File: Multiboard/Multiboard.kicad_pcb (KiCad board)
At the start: 2 copper layers, 120 x 120 mm, 115 parts, among them J1 Conn_01x20_Socket, J2 Conn_01x20_Socket, J3 Debug, J4 USB_C_Receptacle_USB2.0_16P, Q1 Q_NMOS, Q10 Q_NMOS, Q11 Q_NMOS, Q12 Q_NMOS, Q13 Q_NMOS, Q14 Q_NMOS, Q15 Q_NMOS, Q16 Q_NMOS, Q17 Q_NMOS, Q18 Q_NMOS, Q2 Q_NMOS, Q3 Q_NMOS, Q4 Q_NMOS, Q5 Q_NMOS, Q6 Q_NMOS, Q7 Q_NMOS, Q8 Q_NMOS, Q9 Q_NMOS, SW1 BOOT0, SW2 NRST, SW3 SW_SPST, SW4 SW_SPST, SW5 SW_SPST, SW6 SW_SPST, SW7 SW_SPST, SW8 KEY, U1 STM32F411RET6, U2 MAX662AESA_T, U3 MCP1792x-3302xCB, U4 USART1, U5 I2C1, U6 SPI1, U7 ADC, U8 GPIO-PWM, Y1 32.768KHz, Y2 25MHz

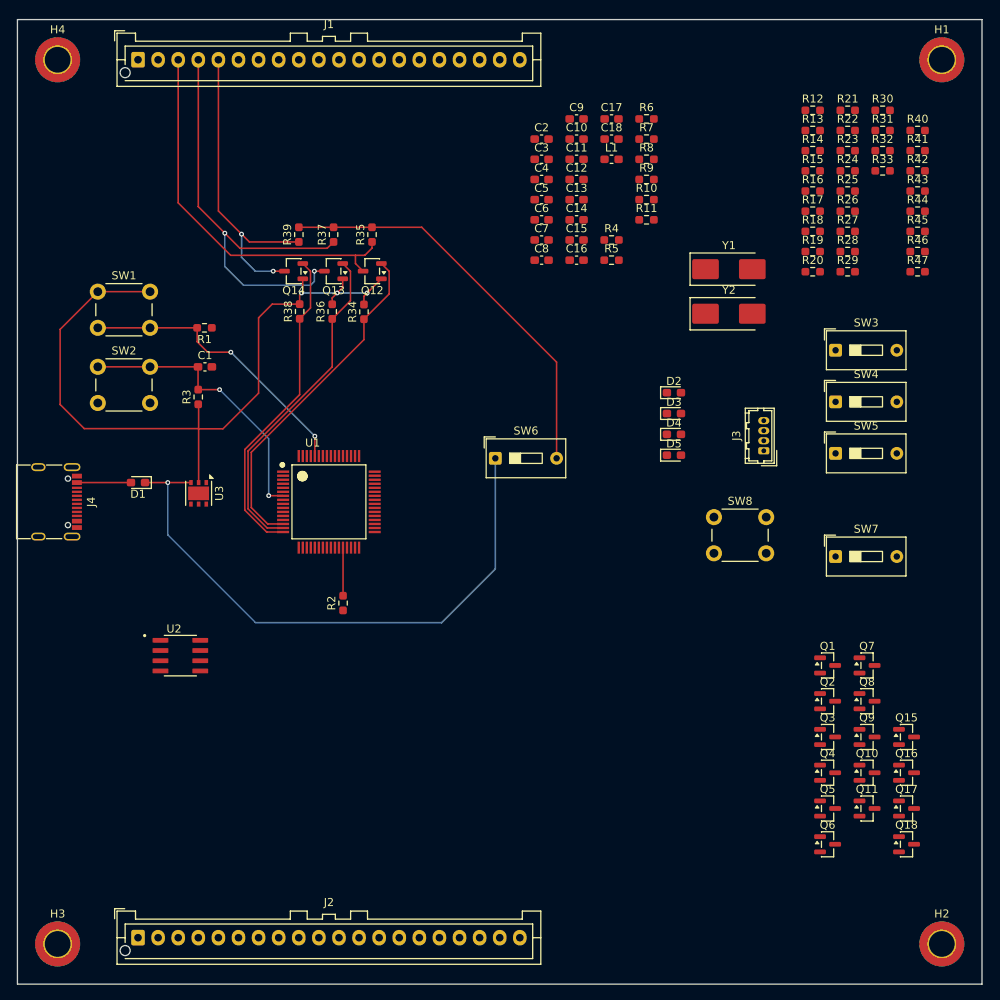
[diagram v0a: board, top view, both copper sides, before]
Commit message: FIxed level shifter implementation
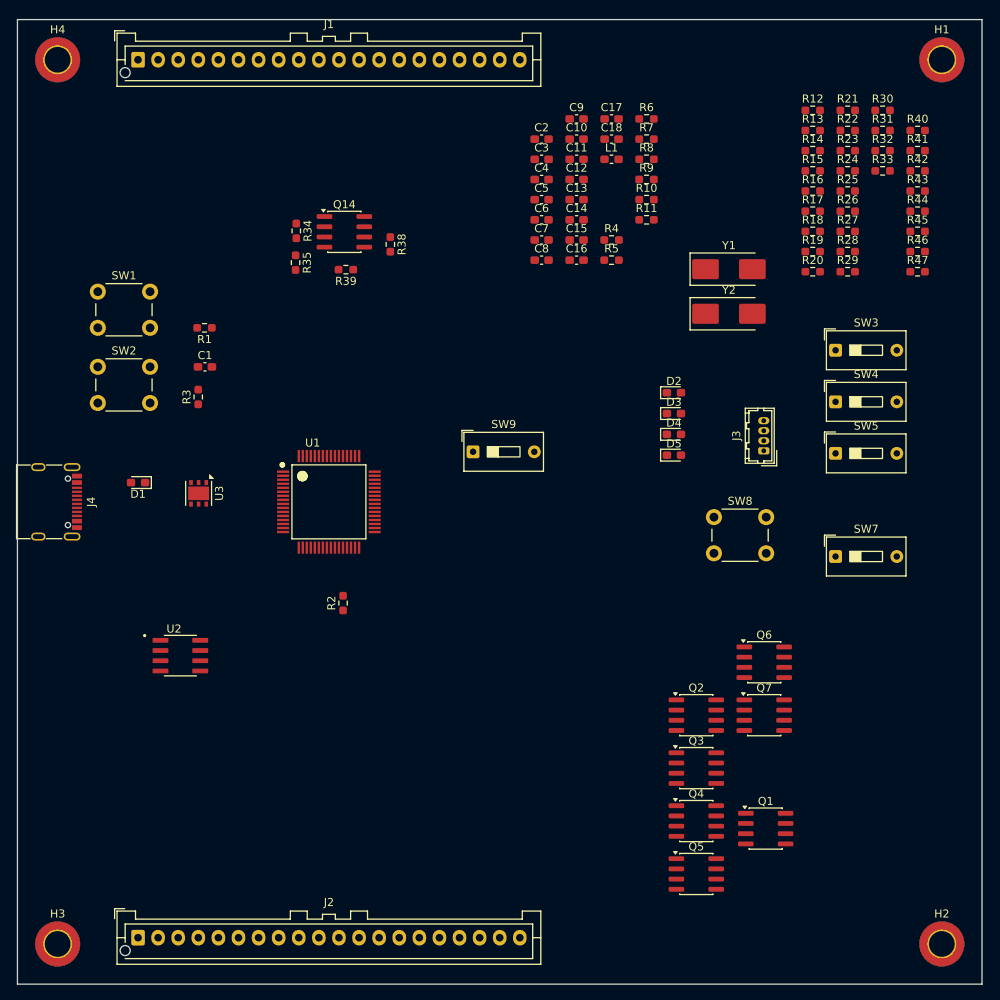
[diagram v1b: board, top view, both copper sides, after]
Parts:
- removed Q10, Q11, Q15, Q16, Q17, Q18, Q8, Q9: Q_NMOS, Package_TO_SOT_SMD:SOT-23
- removed Q12, Q13: Q_NMOS, Package_TO_SOT_SMD:SOT-23-3
- removed R36, R37: 10k, Resistor_SMD:R_0603_1608Metric_Pad0.98x0.95mm_HandSolder
- removed SW6: SW_SPST, Button_Switch_THT:SW_DIP_SPSTx01_Slide_9.78x4.72mm_W7.62mm_P2.54mm
- added SW9: SW_SPST, Button_Switch_THT:SW_DIP_SPSTx01_Slide_9.78x4.72mm_W7.62mm_P2.54mm, F.Cu at (96.7, 93.8)
- Q1, Q2, Q3, Q4, Q5, Q6, Q7: value Q_NMOS -> Q_Dual_NMOS_G1S2G2D2S1D1; footprint Package_TO_SOT_SMD:SOT-23 -> Package_SO:SOIC-8_3.9x4.9mm_P1.27mm
- Q14: value Q_NMOS -> Q_Dual_NMOS_G1S2G2D2S1D1; footprint Package_TO_SOT_SMD:SOT-23-3 -> Package_SO:SOIC-8_3.9x4.9mm_P1.27mm
- moved Q6 24.0 mm to (132.9, 120.0)
- moved Q1 21.7 mm to (133.1, 140.6)
- moved Q5 18.3 mm to (124.5, 146.3)
- moved Q4 17.4 mm to (124.5, 139.7)
- moved Q3 16.8 mm to (124.5, 133.1)
- moved Q2 16.4 mm to (124.5, 126.5)
- moved Q7 14.2 mm to (132.9, 126.5)
- moved R38 14.0 mm to (86.4, 68.0), turned to -90 degrees
- moved R34 13.1 mm to (74.7, 66.3), turned to -90 degrees
- moved R35 10.1 mm to (74.6, 70.2), turned to -90 degrees
- moved Q14 7.98 mm to (80.7, 66.4), turned to 0 degrees
- moved R39 7.30 mm to (80.9, 71.1), turned to 180 degrees
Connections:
- J1 pad 18: PB5-GPIO -> /PB5
- J1 pad 5: PA2-GPIO -> Net-(J1-Pin_5)
- Q1 pad 1: (no net) -> 3V3
- Q1 pad 2: (no net) -> PA10-MCU
- Q1 pad 3: (no net) -> 3V3
- Q2 pad 1: (no net) -> 3V3
- Q2 pad 2: (no net) -> PA12-MCU
- Q2 pad 3: (no net) -> 3V3
- Q3 pad 1: (no net) -> 3V3
- Q3 pad 2: (no net) -> PA5-MCU
- Q3 pad 3: (no net) -> 3V3
- Q4 pad 1: (no net) -> 3V3
- Q4 pad 2: (no net) -> PA7-MCU
- Q4 pad 3: (no net) -> 3V3
- Q5 pad 1: (no net) -> 3V3
- Q5 pad 2: (no net) -> PB7-MCU
- Q5 pad 3: (no net) -> 3V3
- Q6 pad 1: (no net) -> 3V3
- Q6 pad 2: (no net) -> PC7-MCU
- Q6 pad 3: (no net) -> 3V3
- Q7 pad 1: (no net) -> 3V3
- Q7 pad 2: (no net) -> PC9-MCU
- Q7 pad 3: (no net) -> 3V3
- R13 pad 2: Vout -> Net-(SW5-B)
- R15 pad 2: Vout -> Net-(SW5-B)
- R17 pad 2: Vout -> Net-(SW5-B)
- R19 pad 2: Vout -> Net-(SW5-B)
- R21 pad 2: Vout -> Net-(SW3-B)
- R23 pad 2: Vout -> Net-(SW3-B)
- R27 pad 2: Vout -> Net-(SW4-B)
- R29 pad 2: Vout -> Net-(SW4-B)
- R31 pad 2: Vout -> Net-(SW4-B)
- R33 pad 2: Vout -> Net-(SW4-B)
- R35 pad 2: Vout -> Net-(SW9-B)
- R38 pad 1: PA2-MCU -> PA1-GPIO
- R38 pad 2: 3V3 -> Net-(SW9-B)
- R39 pad 1: PA2-GPIO -> PA1-MCU
- R39 pad 2: Vout -> 3V3
- R41 pad 2: Vout -> Net-(SW7-B)
- R43 pad 2: Vout -> Net-(SW7-B)
- R45 pad 2: Vout -> Net-(SW7-B)
- R47 pad 2: Vout -> Net-(SW7-B)
- SW3 pad 2: Vout -> Net-(SW3-B)
- SW4 pad 2: Vout -> Net-(SW4-B)
- SW5 pad 2: Vout -> Net-(SW5-B)
- SW7 pad 2: Vout -> Net-(SW7-B)
- U1 pad 16: PA2-MCU -> Net-(J1-Pin_5)
- U1 pad 57: PB5-MCU -> /PB5
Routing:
- net 3V3: track 94.6 -> 0.07 mm, vias 3 -> 0
- net 5V: track 74.0 -> 0.00 mm, vias 1 -> 0
- net PA1-GPIO: track 56.6 -> 0.00 mm, vias 2 -> 0
- net Vout: track 51.0 -> 0.00 mm
- net PA0-GPIO: track 48.1 -> 0.00 mm
- net PA0-MCU: track 42.7 -> 0.00 mm
- net PA1-MCU: track 41.5 -> 0.00 mm
- net PA2-MCU: track 40.4 -> 0.00 mm
- net PA2-GPIO: track 39.4 -> 0.00 mm, vias 2 -> 0
- net Net-(U1-BOOT0): track 36.1 -> 0.00 mm, vias 2 -> 0
- net Net-(U1-NRST): track 35.5 -> 0.07 mm, vias 2 -> 0
- net Net-(D1-A): track 6.73 -> 0.00 mm
- net Net-(U1-PB2): track 5.98 -> 0.01 mm

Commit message: Fixed bus implementation
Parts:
- moved R35 13.9 mm to (87.3, 64.5), turned to 0 degrees
- moved R34 12.6 mm to (87.3, 67.0), turned to 0 degrees
- moved R38 12.6 mm to (73.9, 65.8), turned to 180 degrees
- moved R39 8.92 mm to (77.3, 62.9)
- turned Q14 to 180 degrees

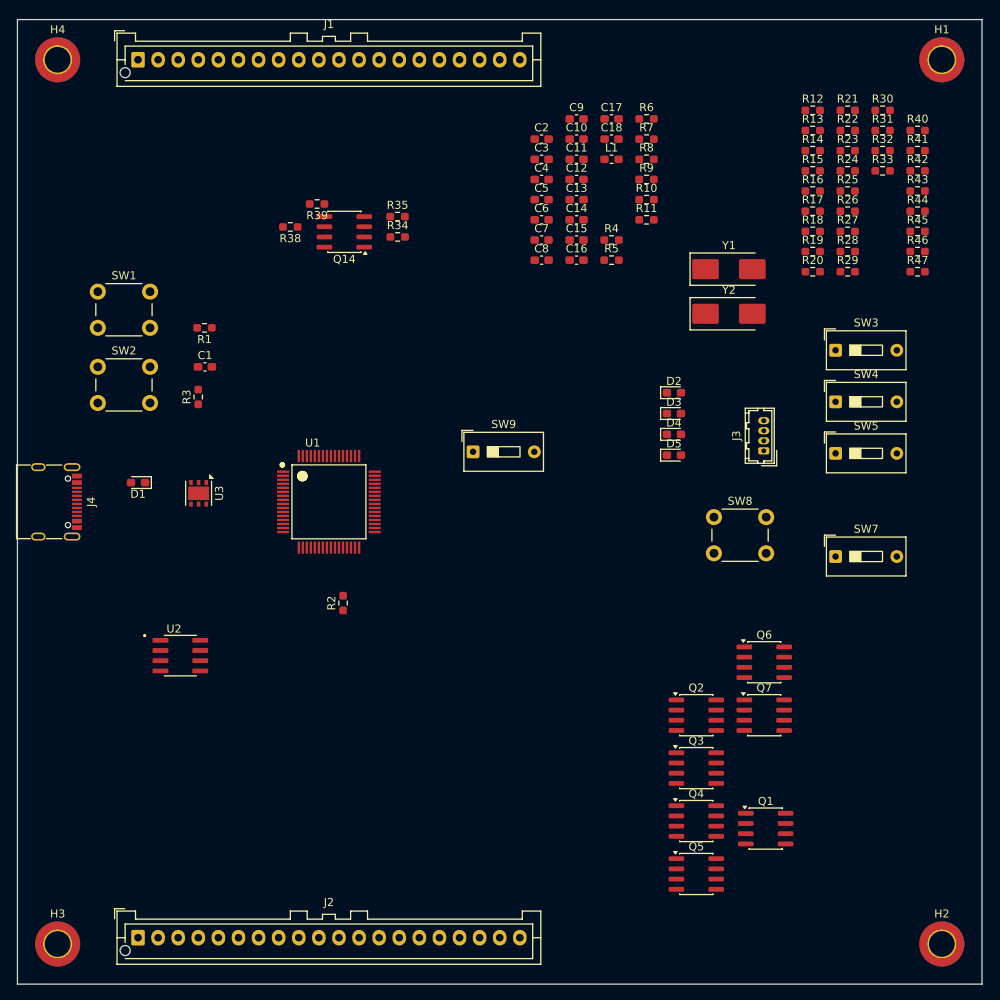
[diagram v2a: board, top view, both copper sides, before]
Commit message: changed mosfet footprint
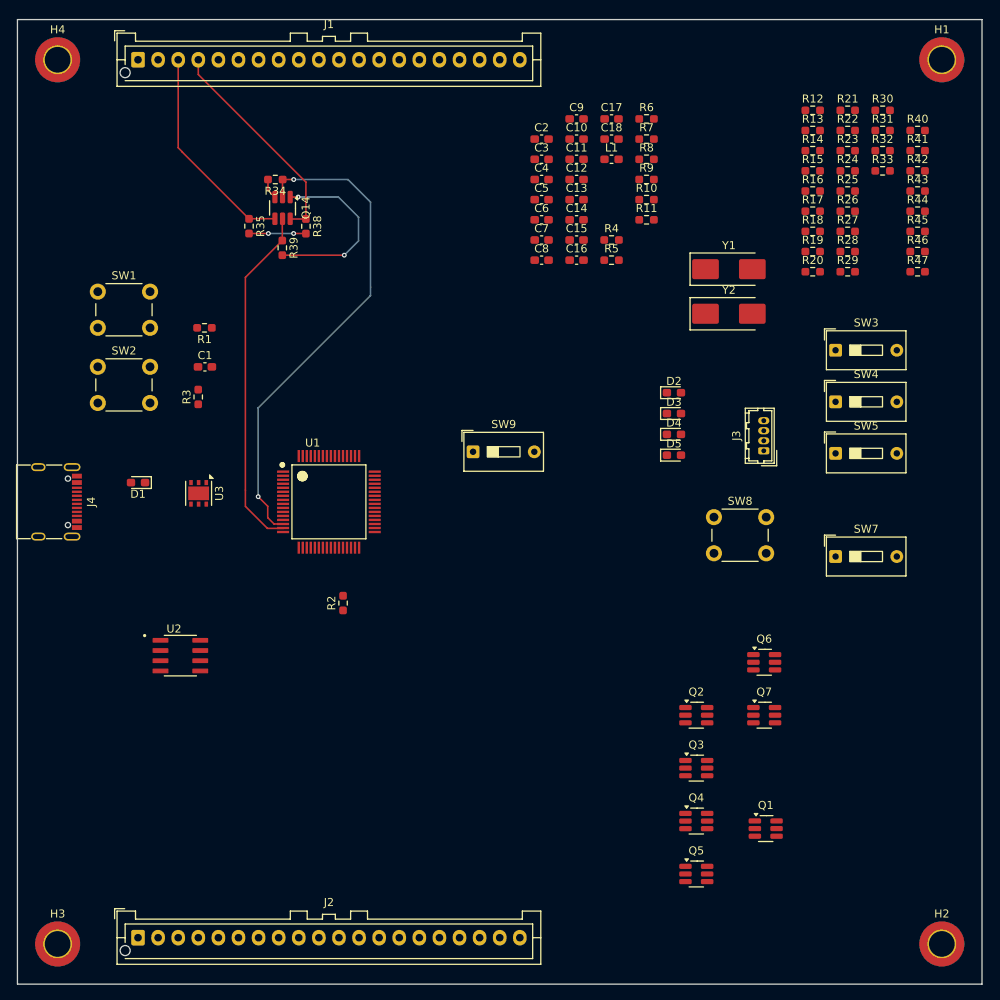
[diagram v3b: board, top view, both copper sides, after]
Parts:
- Q1, Q14, Q2, Q3, Q4, Q5, Q6, Q7: footprint Package_SO:SOIC-8_3.9x4.9mm_P1.27mm -> Package_TO_SOT_SMD:SOT-23-6_Handsoldering
- moved R35 18.5 mm to (68.8, 65.7), turned to -90 degrees
- moved R34 16.8 mm to (72.1, 59.9), turned to 180 degrees
- moved Q14 8.25 mm to (73.0, 63.4), turned to -90 degrees
- moved R39 6.97 mm to (73.0, 68.4), turned to -90 degrees
- moved R38 1.94 mm to (75.9, 65.7), turned to -90 degrees
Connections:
- net /PA15 renamed Net-(J2-Pin_3)
- net /PA3 renamed Net-(J1-Pin_6)
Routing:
- net PA0-MCU: track 0.00 -> 62.1 mm, vias 0 -> 2
- net PA1-MCU: track 0.00 -> 43.6 mm
- net PA1-GPIO: track 0.01 -> 27.3 mm
- net PA0-GPIO: track 0.01 -> 26.7 mm
- net 3V3: track 0.07 -> 25.3 mm, vias 0 -> 2
- net Net-(SW9-B): track 0.00 -> 7.09 mm, vias 0 -> 2

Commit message: positioned and wired adc level shifter and decoupling capacitors
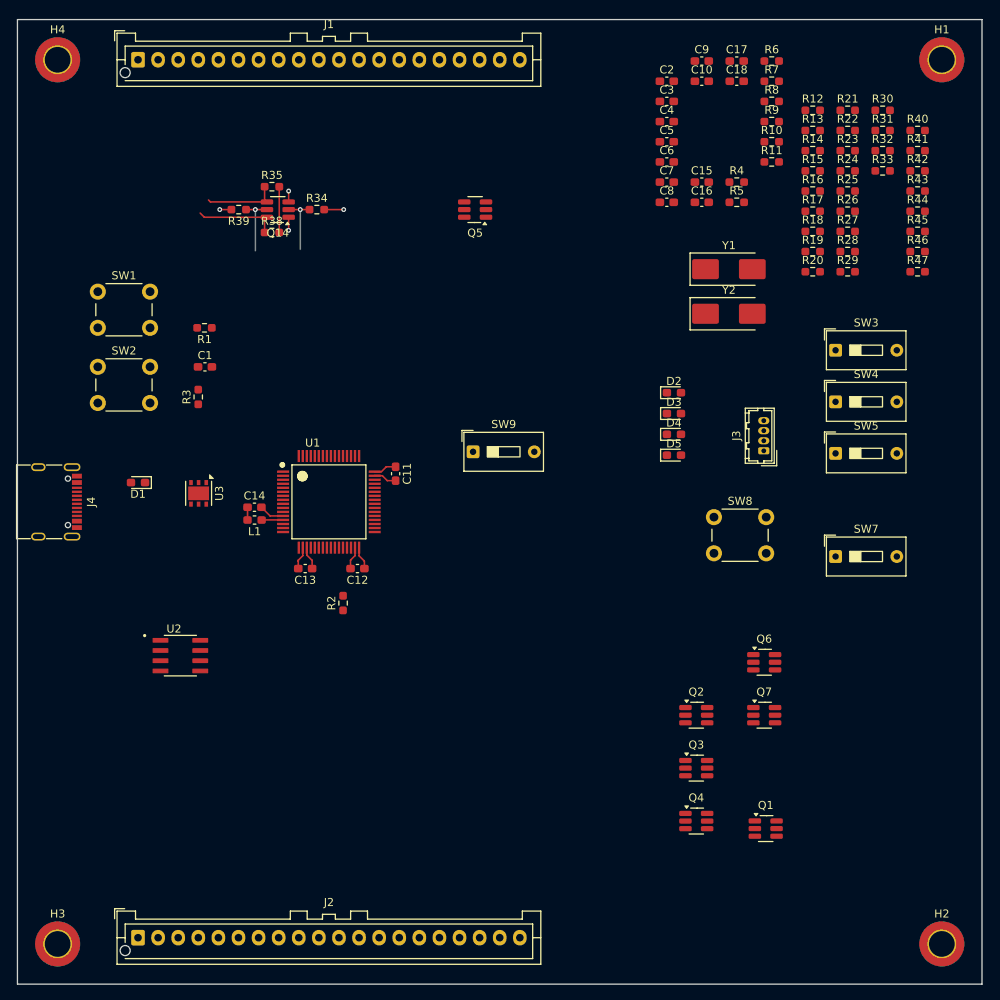
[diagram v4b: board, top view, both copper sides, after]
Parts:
- moved Q5 87.1 mm to (96.9, 63.6), turned to 180 degrees
- moved L1 63.1 mm to (69.5, 102.3), turned to 180 degrees
- moved C13 57.0 mm to (75.8, 108.3), turned to 180 degrees
- moved C12 55.6 mm to (82.3, 108.3), turned to 180 degrees
- moved C14 53.7 mm to (69.5, 100.7)
- moved C11 45.1 mm to (87.0, 96.5), turned to -90 degrees
- moved C17 17.2 mm to (129.5, 45.2)
- moved R4 17.2 mm to (129.5, 60.2)
- moved R5 17.2 mm to (129.5, 62.7)
- moved C18 17.2 mm to (129.5, 47.7)
- moved C15 17.2 mm to (125.1, 60.2)
- moved C16 17.2 mm to (125.1, 62.7)
- moved C9 17.2 mm to (125.1, 45.2)
- moved R6 17.2 mm to (133.8, 45.2)
- moved R8 17.2 mm to (133.8, 50.2)
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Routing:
- net PA0-MCU: track 62.1 -> 7.54 mm, vias 2 -> 1
- net PA1-MCU: track 43.6 -> 7.72 mm, vias 0 -> 1
- net PA0-GPIO: track 26.7 -> 9.39 mm
- net PA1-GPIO: track 27.3 -> 10.5 mm
- net GND: track 0.00 -> 11.7 mm
- net 3V3: track 25.3 -> 15.5 mm, vias 2 -> 4
- net Net-(U1-VDDA/VREF+): track 0.00 -> 2.72 mm
- net /VREF+: track 0.00 -> 1.51 mm
- net Net-(SW9-B): track 7.09 -> 5.70 mm, vias 2 -> 0

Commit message: positioned USART1 and I2C1 level shifters
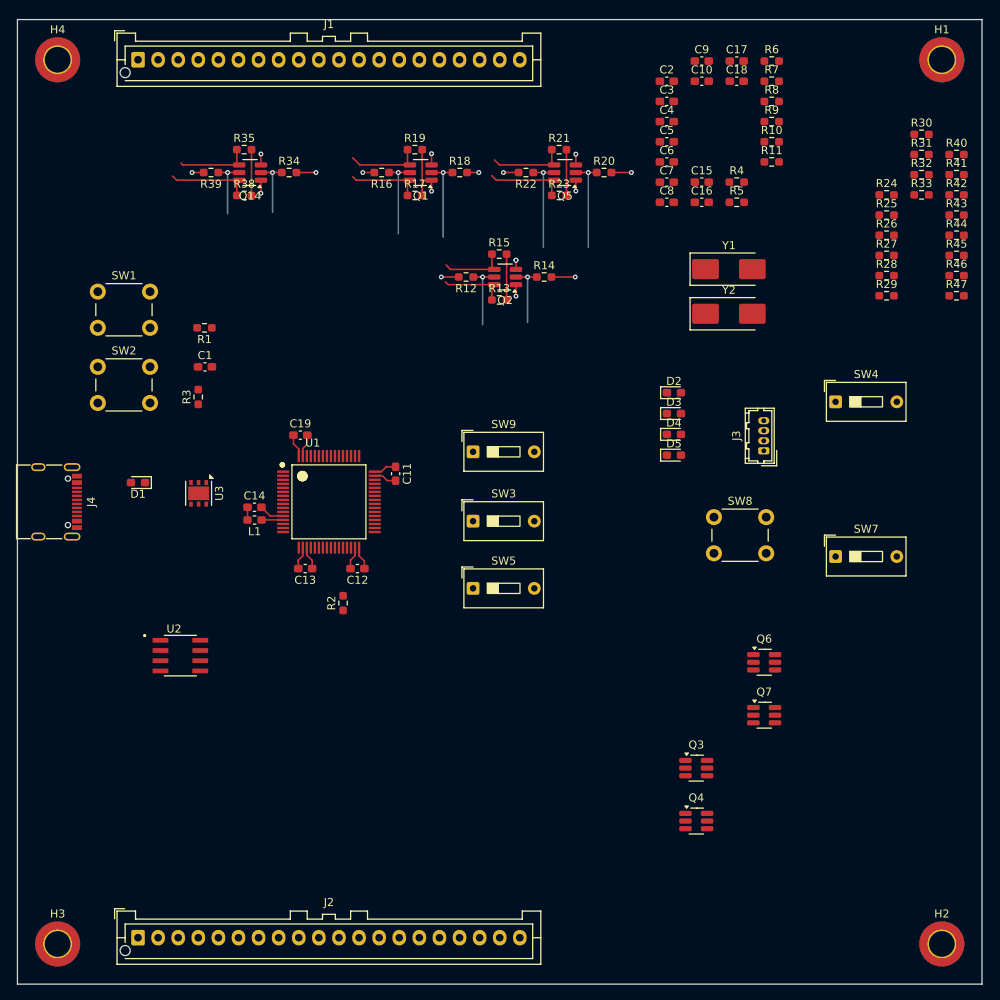
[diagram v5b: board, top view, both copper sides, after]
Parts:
- added C19: 0.1u, Capacitor_SMD:C_0603_1608Metric_Pad1.08x0.95mm_HandSolder, F.Cu at (75.2, 91.7)
- moved Q1 92.2 mm to (90.2, 59.0), turned to 180 degrees
- moved Q2 59.5 mm to (100.7, 72.0), turned to 180 degrees
- moved R16 53.7 mm to (85.3, 59.0), turned to 180 degrees
- moved R19 51.1 mm to (89.4, 56.2)
- moved SW3 49.9 mm to (96.7, 102.4)
- moved R17 49.5 mm to (89.4, 61.9)
- moved SW5 48.1 mm to (96.7, 110.8)
- moved R12 47.9 mm to (95.8, 72.0), turned to 180 degrees
- moved R18 44.5 mm to (95.0, 59.0)
- moved R13 44.3 mm to (99.9, 74.9)
- moved R22 40.4 mm to (103.3, 59.0), turned to 180 degrees
- moved R15 40.3 mm to (99.9, 69.2)
- moved R14 36.9 mm to (105.5, 72.0)
- moved R23 36.3 mm to (107.4, 61.9)
- moved R21 36.2 mm to (107.4, 56.2)
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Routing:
- net 3V3: track 15.5 -> 38.9 mm, vias 4 -> 17
- net PB7-MCU: track 0.00 -> 11.9 mm, vias 0 -> 1
- net PB6-MCU: track 0.00 -> 11.9 mm, vias 0 -> 1
- net Net-(SW5-B): track 0.00 -> 11.4 mm
- net PA10-MCU: track 0.00 -> 10.6 mm, vias 0 -> 1
- net PA9-MCU: track 0.00 -> 10.2 mm, vias 0 -> 1
- net PB6-GPIO: track 0.00 -> 10.1 mm
- net PB7-GPIO: track 0.00 -> 9.72 mm
- net PA10-GPIO: track 0.00 -> 9.50 mm
- net PA9-GPIO: track 0.00 -> 9.31 mm
- net PA11-MCU: track 0.00 -> 8.52 mm, vias 0 -> 1
- net PA11-GPIO: track 0.00 -> 8.26 mm
- net PA12-MCU: track 0.00 -> 8.25 mm, vias 0 -> 1
- net PA12-GPIO: track 0.00 -> 8.24 mm
- net Net-(SW3-B): track 0.00 -> 5.70 mm
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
